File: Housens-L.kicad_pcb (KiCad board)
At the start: 4 copper layers, 50 x 50 mm, 35 parts, among them J1 JTAG/SWD, J2 USB_C_2.0, SW1 RESET, U1 MCP1603, U2 BME280, U3 OPT3005, U4 STM32WB55CGUx

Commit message: Layout antenna
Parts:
- added Y1: 32MHz, Crystal:Crystal_SMD_2520-4Pin_2.5x2.0mm, F.Cu at (82.2, 111.2)
- added Y2: 32.768kHz, Crystal:Crystal_SMD_2520-4Pin_2.5x2.0mm, F.Cu at (88.2, 98.7)
- D1: value D -> D_Schottky
- moved L2 21.6 mm to (85.8, 115.8), turned to 90 degrees
- moved C6 20.2 mm to (82.3, 114.8), turned to 90 degrees
- moved C16 14.5 mm to (77.6, 110.0), turned to -90 degrees
- moved C13 13.9 mm to (86.6, 111.2), turned to -90 degrees
- moved C15 12.5 mm to (79.3, 110.0), turned to -90 degrees
- moved C12 11.5 mm to (84.3, 99.0), turned to 90 degrees
- moved C9 10.7 mm to (91.2, 102.2), turned to 0 degrees
- moved C7 10.4 mm to (75.8, 110.0)
- moved C8 10.2 mm to (88.4, 111.2), turned to -90 degrees
- moved C14 9.64 mm to (91.1, 106.3)
- moved C10 9.08 mm to (74.2, 110.0)
- moved C11 8.30 mm to (82.6, 99.0), turned to 90 degrees
- moved AE1 4.39 mm to (65.7, 106.2)
- moved U4 0.50 mm to (85.0, 105.0), turned to -90 degrees
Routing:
- net +1V8: track 0.00 -> 26.7 mm, vias 0 -> 2
- net GND: track 6.08 -> 31.0 mm, vias 4 -> 94
- net Net-(AE1-A): track 0.00 -> 15.8 mm
- net Net-(U4-VFBSMPS): track 0.00 -> 9.63 mm
- net Net-(U4-VLXSMPS): track 0.00 -> 8.40 mm
- net Net-(U4-NRST): track 0.00 -> 7.12 mm, vias 0 -> 1
- net Net-(U4-OSC_IN): track 0.00 -> 3.84 mm
- net Net-(U4-PC14): track 0.00 -> 3.00 mm
- net Net-(U4-OSC_OUT): track 0.00 -> 2.78 mm
- net Net-(U4-PC15): track 0.00 -> 2.31 mm
- net +BATT: track 0.00 -> 1.97 mm
- net /USB_D_P: track 0.00 -> 0.62 mm, vias 0 -> 1
- net /USB_D_N: track 0.00 -> 0.62 mm, vias 0 -> 1
- net /SPI1_NSS: track 0.00 -> 0.60 mm, vias 0 -> 1
- net /SPI1_MOSI: track 0.00 -> 0.60 mm, vias 0 -> 1
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- added copper zone on F.Cu, net Net-(AE1-A)

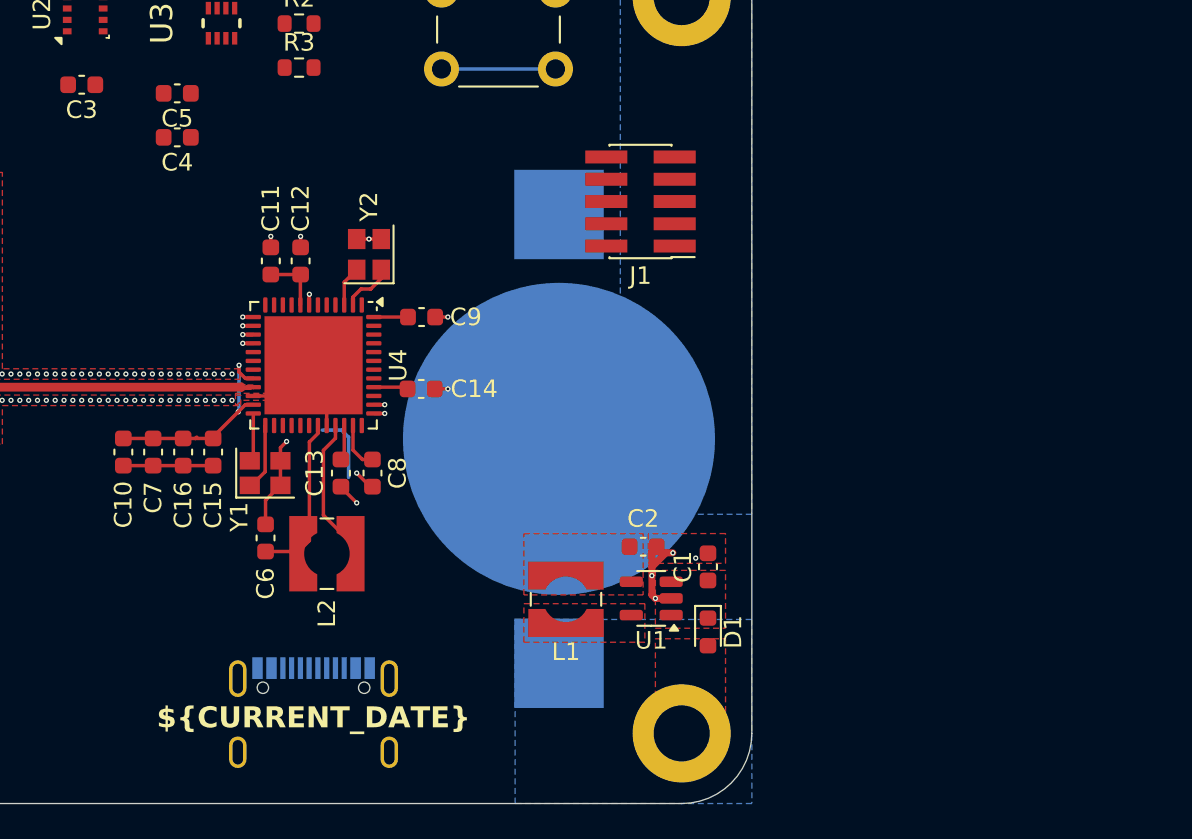
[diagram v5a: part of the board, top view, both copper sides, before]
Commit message: Add fuel gauge
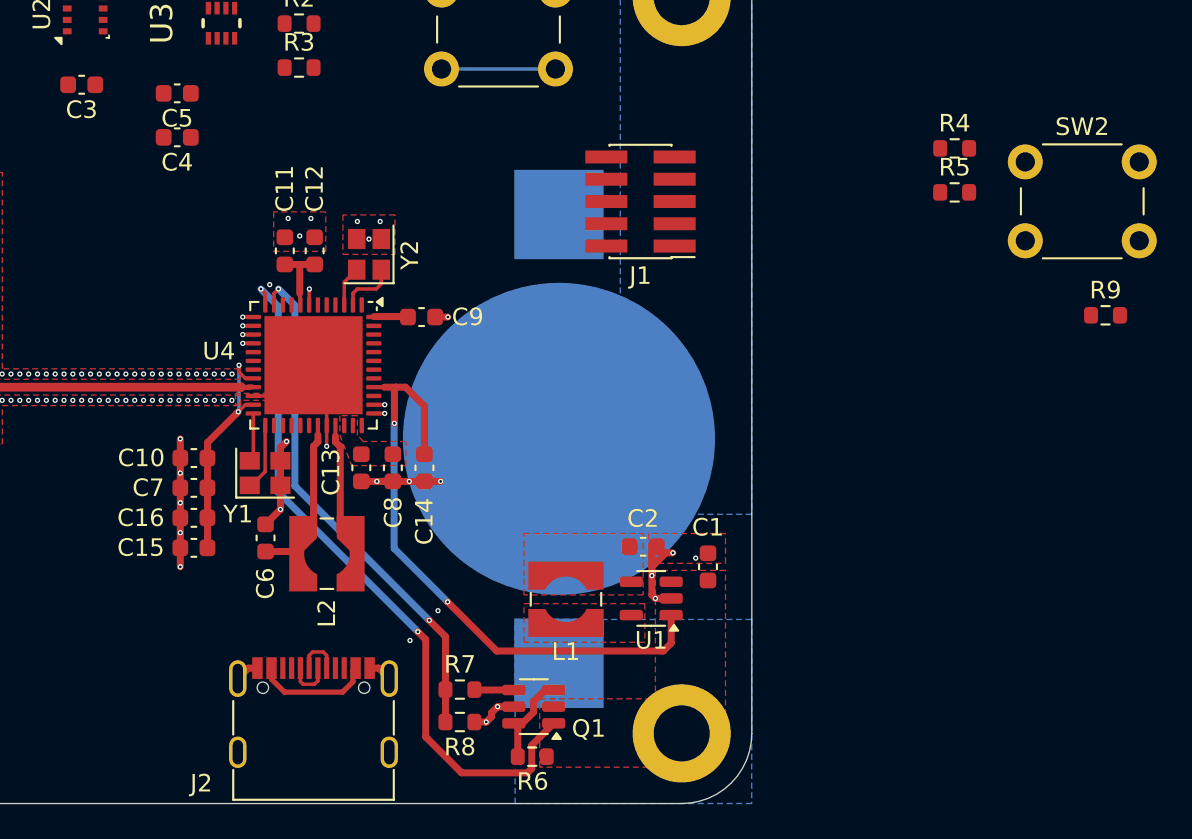
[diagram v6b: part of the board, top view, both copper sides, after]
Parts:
- removed D1: D_Schottky, Diode_SMD:D_0603_1608Metric
- added Q1: DMC3071LVT, Package_TO_SOT_SMD:TSOT-23-6, F.Cu at (97.6, 124.5)
- added R4: 100k, Resistor_SMD:R_0603_1608Metric, F.Cu at (121.6, 92.6)
- added R5: 10k, Resistor_SMD:R_0603_1608Metric, F.Cu at (121.6, 95.1)
- added R6: 10k, Resistor_SMD:R_0603_1608Metric, F.Cu at (97.5, 127.3)
- added R7: 24k, Resistor_SMD:R_0603_1608Metric, F.Cu at (93.3, 123.5)
- added R8: 27k, Resistor_SMD:R_0603_1608Metric, F.Cu at (93.3, 125.3)
- added R9: 10k, Resistor_SMD:R_0603_1608Metric, F.Cu at (130.2, 102.2)
- added SW2: USER_BTN, Button_Switch_THT:SW_PUSH_6mm, F.Cu at (125.6, 93.4)
- J2: moved to F.Cu
- moved C15 5.58 mm to (78.2, 115.4), turned to 180 degrees
- moved C14 4.50 mm to (91.3, 110.8), turned to -90 degrees
- moved C10 4.04 mm to (78.2, 110.3), turned to 180 degrees
- moved C16 3.81 mm to (78.2, 113.7), turned to 180 degrees
- moved C7 3.10 mm to (78.2, 112.0), turned to 180 degrees
- moved C8 1.20 mm to (89.5, 110.8)
- moved C13 1.20 mm to (87.7, 110.8)
- moved C11 0.99 mm to (83.4, 98.5)
- moved C12 0.99 mm to (85.1, 98.5)
- turned J2 to 0 degrees
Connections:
- BT1 pad 1: /CELL -> +BATT
- H3 pad 1: /CELL -> +BATT
- U4 pad 11: unconnected-(U4-PA2-Pad11) -> /FUEL_ADC
- U4 pad 12: unconnected-(U4-PA3-Pad12) -> /FUEL_CTL
- U4 pad 30: unconnected-(U4-PE4-Pad30) -> /USB_DETECT
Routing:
- net /FUEL_CTL: track 0.00 -> 40.6 mm, vias 0 -> 2
- net +BATT: track 1.97 -> 34.7 mm, vias 0 -> 2
- net /FUEL_ADC: track 0.00 -> 29.7 mm, vias 0 -> 2
- net GND: track 31.0 -> 39.2 mm, vias 94 -> 109
- net +1V8: track 26.7 -> 19.6 mm
- net Net-(J2-VBUS-PadA4): track 0.00 -> 6.67 mm
- net Net-(Q1A-D): track 0.00 -> 5.41 mm
- net /USB_D_N: track 0.62 -> 3.26 mm
- net /USB_D_P: track 0.62 -> 3.24 mm
- net Net-(Q1B-D): track 0.00 -> 2.26 mm
- net Net-(U4-VLXSMPS): track 8.40 -> 7.24 mm
- net Net-(U4-VFBSMPS): track 9.63 -> 8.99 mm
- added copper zone on B.Cu, net +BATT
- removed copper zone on B.Cu, net /CELL
- removed copper zone on F.Cu, net /CELL

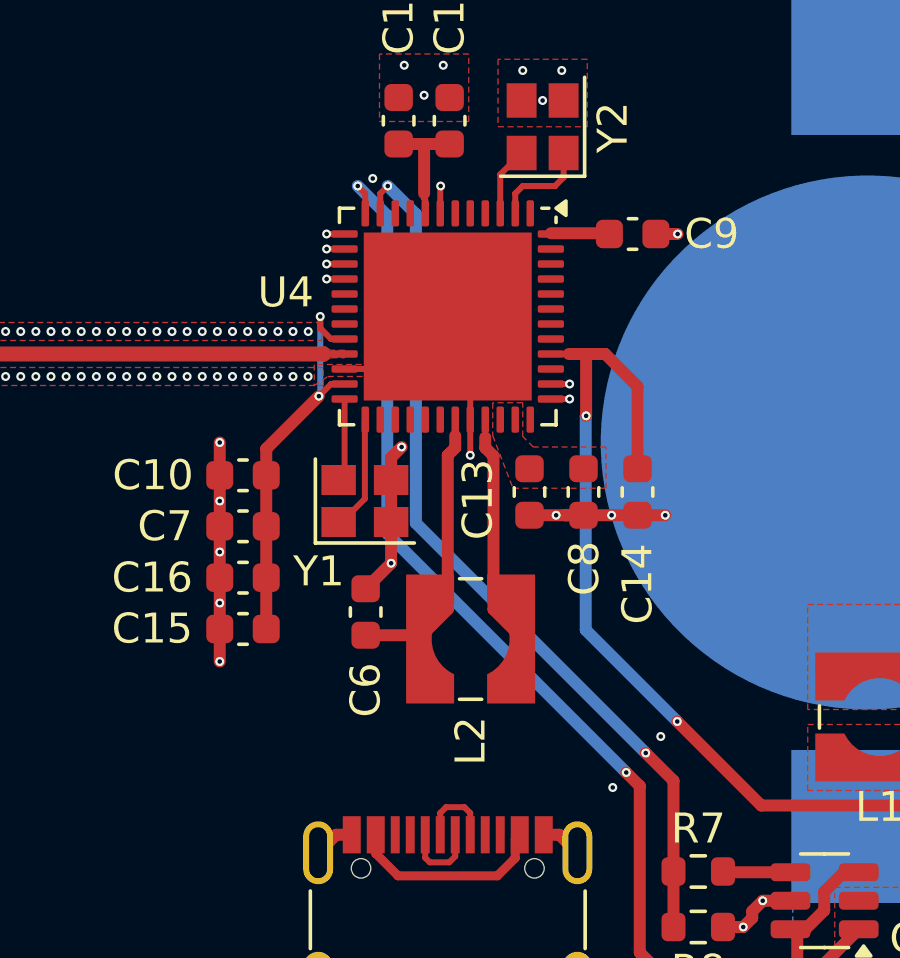
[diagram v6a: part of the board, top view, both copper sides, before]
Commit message: Custom thermal footprint for MCU
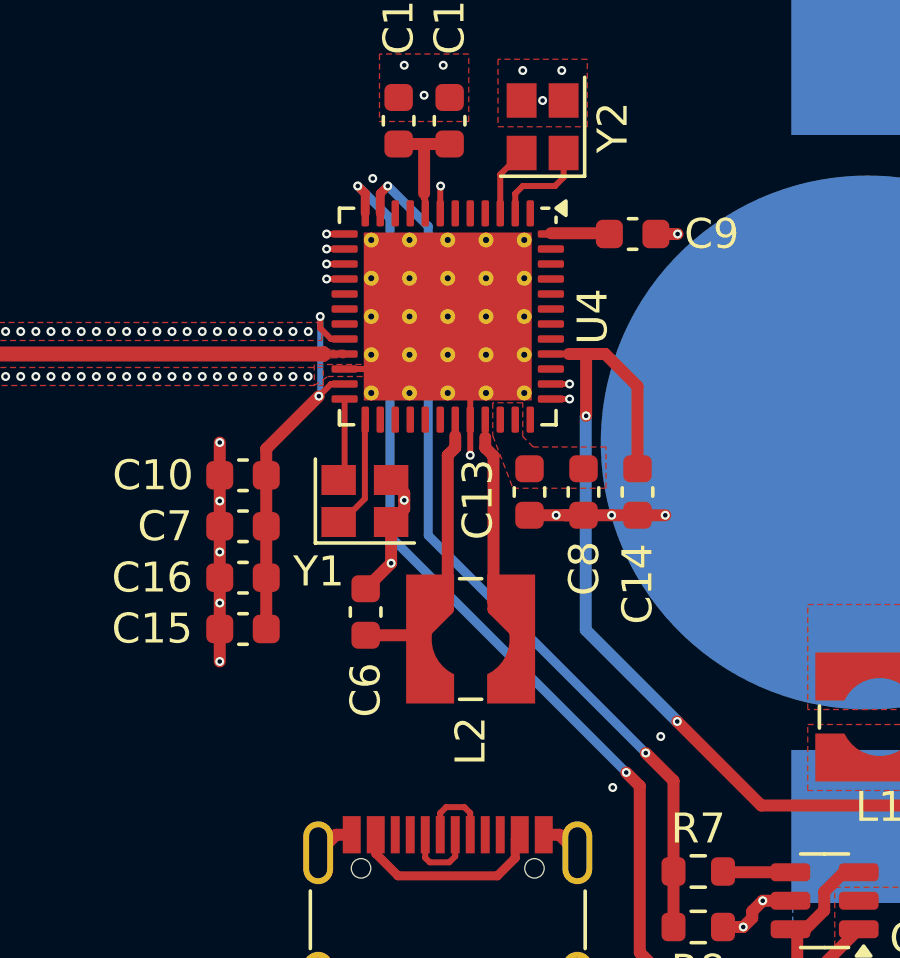
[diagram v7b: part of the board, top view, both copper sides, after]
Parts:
- U4: footprint Package_DFN_QFN:QFN-48-1EP_7x7mm_P0.5mm_EP5.6x5.6mm -> Invented:QFN-48-1EP_7x7mm_P0.5mm_EP5.6x5.6mm_ThermalVias_OneSided
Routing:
- net GND: track 39.2 -> 38.4 mm

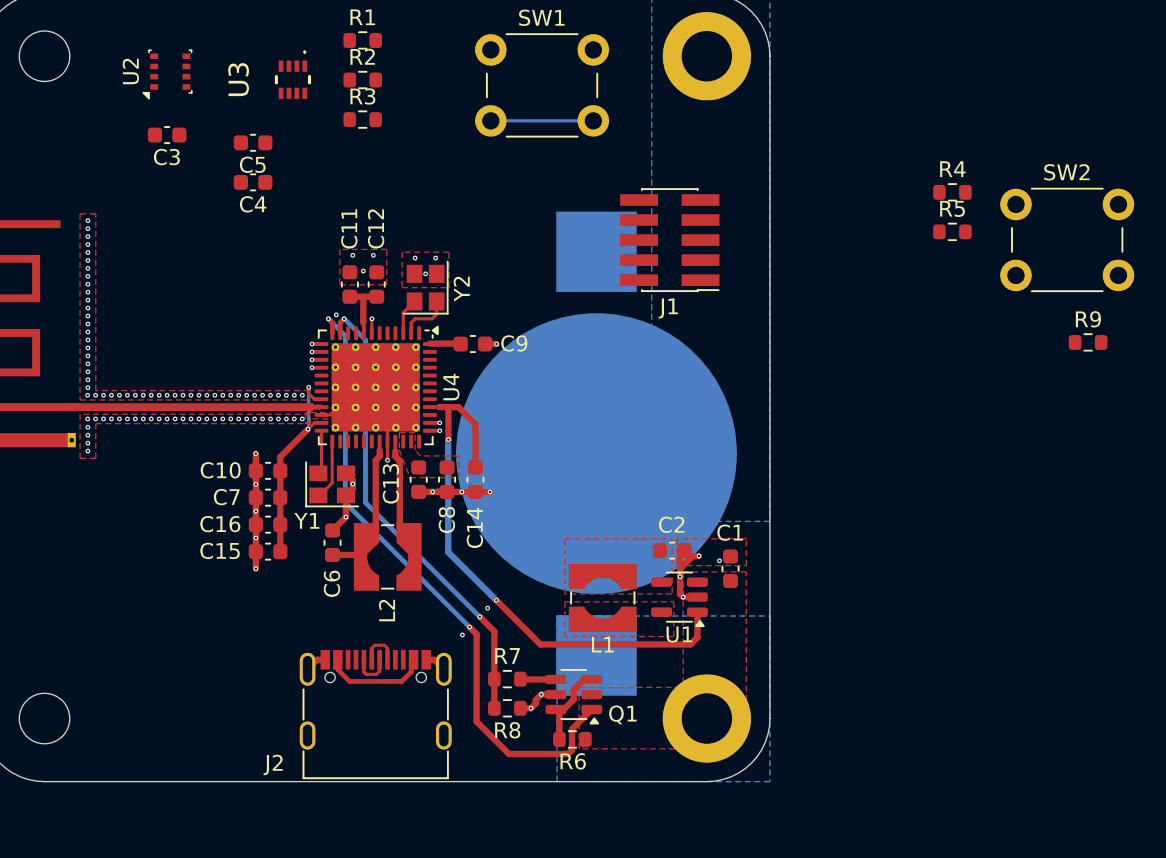
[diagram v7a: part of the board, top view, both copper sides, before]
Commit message: Layout 1V8 and USB
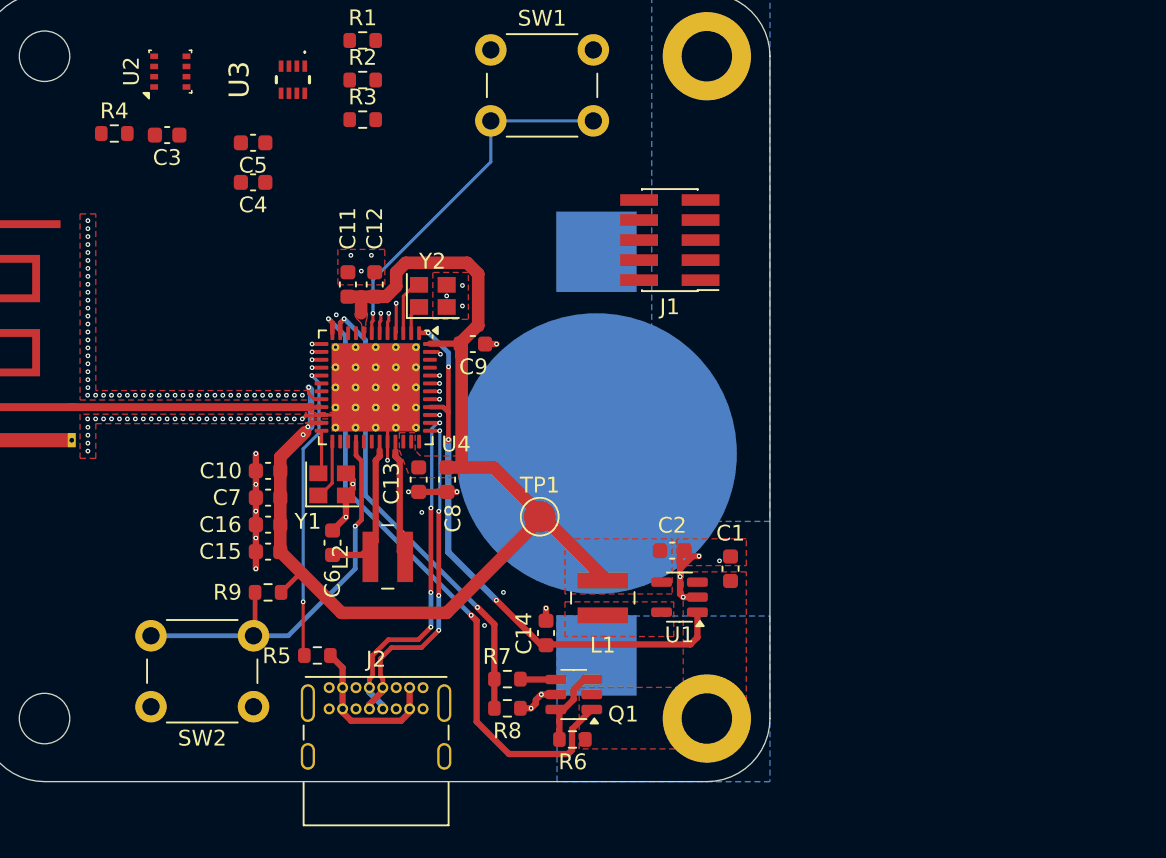
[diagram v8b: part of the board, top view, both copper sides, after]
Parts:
- added TP1: TestPoint, TestPoint:TestPoint_Pad_D2.0mm, F.Cu at (95.4, 113.2)
- J2: footprint Connector_USB:USB_C_Receptacle_G-Switch_GT-USB-7010ASV -> Connector_USB:USB_C_Receptacle_GCT_USB4085
- L1, L2: footprint Inductor_SMD:L_Wuerth_WE-TPC-3816 -> Imported:L_Wuerth_WE-TPC-2811
- moved SW2 57.9 mm to (77.2, 125.2), turned to 180 degrees
- moved R9 54.4 mm to (78.2, 118.0), turned to 180 degrees
- moved R4 53.3 mm to (68.4, 88.9)
- moved R5 48.4 mm to (81.3, 122.0)
- moved C14 10.7 mm to (95.8, 120.6), turned to 90 degrees
- moved J2 3.54 mm to (82.0, 124.0)
- moved Y2 0.70 mm to (88.6, 99.2), turned to 0 degrees
- moved C11 0.12 mm to (83.2, 98.5)
- moved C12 0.12 mm to (84.9, 98.5)
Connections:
- J1 pad 1: +BATT -> +1V8
- U4 pad 17: unconnected-(U4-PA8-Pad17) -> /USB_DETECT
- U4 pad 28: unconnected-(U4-PB0-Pad28) -> /USER_BTN
- U4 pad 30: /USB_DETECT -> unconnected-(U4-PE4-Pad30)
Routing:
- net +1V8: track 19.6 -> 77.6 mm, vias 2 -> 3
- net /USER_BTN: track 0.00 -> 25.9 mm, vias 0 -> 1
- net /USB_DETECT: track 0.00 -> 19.0 mm, vias 0 -> 2
- net /USB_D_P: track 3.24 -> 22.2 mm, vias 1 -> 4
- net /USB_D_N: track 3.26 -> 21.4 mm, vias 1 -> 4
- net Net-(U4-NRST): track 7.42 -> 23.1 mm
- net Net-(J2-VBUS-PadA4): track 6.67 -> 10.2 mm
- net GND: track 38.4 -> 36.3 mm, vias 109 -> 110
- net /BOOT0: track 0.00 -> 1.92 mm, vias 0 -> 1
- net +BATT: track 34.7 -> 36.4 mm, vias 2 -> 4
- net Net-(U4-PC14): track 3.31 -> 1.87 mm
- net Net-(U4-PC15): track 2.31 -> 3.64 mm
- net /I2C1_SCL: track 0.00 -> 1.29 mm, vias 0 -> 1
- net /OPT_INT: track 0.00 -> 1.29 mm, vias 0 -> 1
- net /I2C1_SDA: track 0.00 -> 0.73 mm, vias 0 -> 1
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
